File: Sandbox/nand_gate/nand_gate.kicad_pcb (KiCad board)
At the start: 2 copper layers, 63.5 x 33 mm, 11 parts, among them Q1 2N3904, Q2 2N3904, Q3 2N3904, SW1 SW_SPST, SW2 SW_SPST

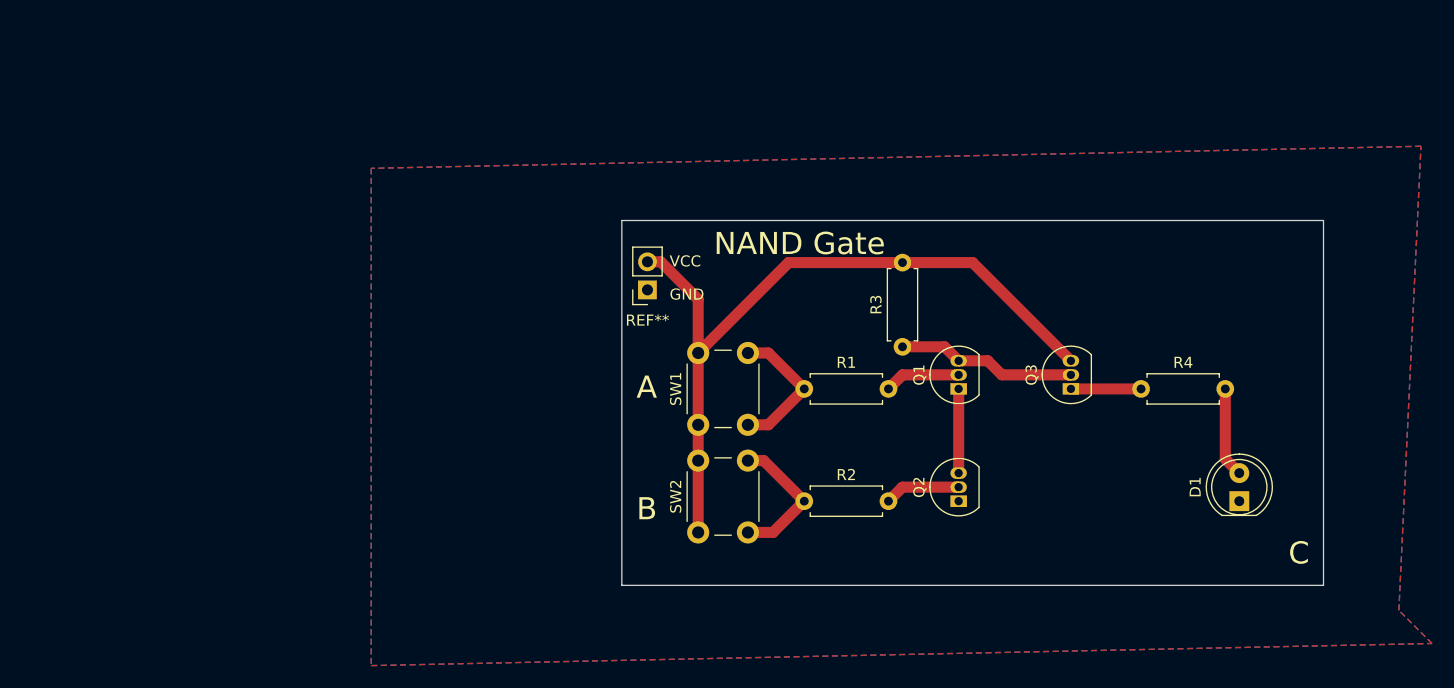
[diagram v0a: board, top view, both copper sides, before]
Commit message: Layout for nand gate
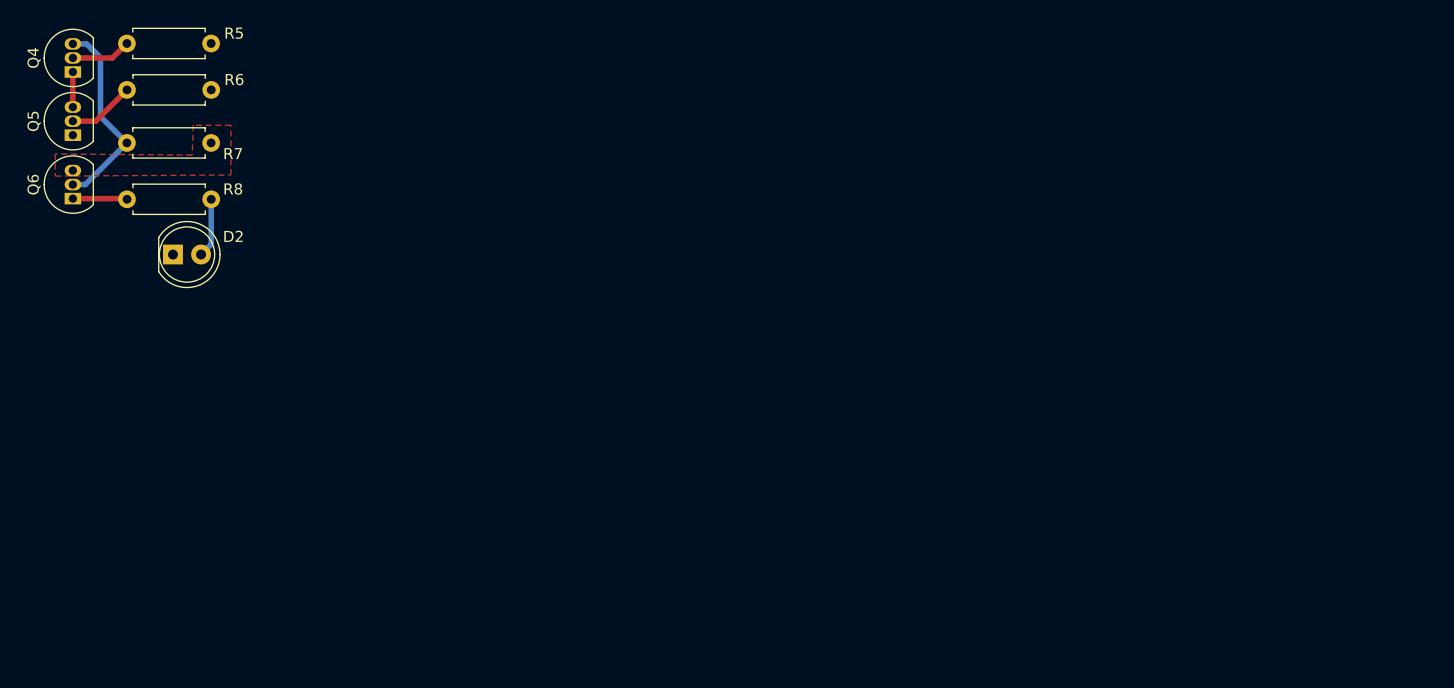
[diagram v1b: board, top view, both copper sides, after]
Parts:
- removed D1: LED, LED_THT:LED_D5.0mm
- removed Q1, Q2, Q3: 2N3904, Package_TO_SOT_THT:TO-92_Inline
- removed R1, R2, R3: 1k, Resistor_THT:R_Axial_DIN0207_L6.3mm_D2.5mm_P7.62mm_Horizontal
- removed R4: 150, Resistor_THT:R_Axial_DIN0207_L6.3mm_D2.5mm_P7.62mm_Horizontal
- removed REF**: PinSocket_1x02_P2.54mm_Vertical, Connector_PinSocket_2.54mm:PinSocket_1x02_P2.54mm_Vertical
- removed SW1, SW2: SW_SPST, Button_Switch_THT:SW_PUSH_6mm
- added D2: LED, LED_THT:LED_D5.0mm, F.Cu at (66.1, 48.8)
- added Q4: 2N3904, Package_TO_SOT_THT:TO-92_Inline, F.Cu at (57.0, 32.3)
- added Q5: 2N3904, Package_TO_SOT_THT:TO-92_Inline, F.Cu at (57.0, 38.0)
- added Q6: 2N3904, Package_TO_SOT_THT:TO-92_Inline, F.Cu at (57.0, 43.7)
- added R5: 1k, Resistor_THT:R_Axial_DIN0207_L6.3mm_D2.5mm_P7.62mm_Horizontal, F.Cu at (69.5, 29.7)
- added R6: 1k, Resistor_THT:R_Axial_DIN0207_L6.3mm_D2.5mm_P7.62mm_Horizontal, F.Cu at (69.5, 33.9)
- added R7: 1k, Resistor_THT:R_Axial_DIN0207_L6.3mm_D2.5mm_P7.62mm_Horizontal, F.Cu at (61.9, 38.7)
- added R8: 150, Resistor_THT:R_Axial_DIN0207_L6.3mm_D2.5mm_P7.62mm_Horizontal, F.Cu at (61.9, 43.8)
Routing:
- net VCC: track 67.9 -> 0.00 mm
- net Net-(Q4-C): track 0.00 -> 18.2 mm
- net Net-(Q1-C): track 16.3 -> 0.00 mm
- net /B: track 13.5 -> 0.00 mm
- net /A: track 12.9 -> 0.00 mm
- net /C: track 8.15 -> 0.00 mm
- net Net-(Q1-E): track 7.62 -> 0.00 mm
- net Net-(Q2-B): track 6.88 -> 0.00 mm
- net Net-(Q1-B): track 6.88 -> 0.00 mm
- net Net-(Q3-E): track 6.35 -> 0.00 mm
- net Net-(Q5-B): track 0.00 -> 6.07 mm
- net Net-(Q4-B): track 0.00 -> 5.43 mm
- net /D-Flip Flop/D-Latch/SR-Latch/nand_gate/C: track 0.00 -> 5.38 mm
- net Net-(Q6-E): track 0.00 -> 4.92 mm
- net Net-(Q4-E): track 0.00 -> 3.18 mm
- added copper zone on F.Cu, net VCC
- removed copper zone on B.Cu, net GND
- removed copper zone on F.Cu, net GND
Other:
- board outline removed
- board text removed: "A"
- board text removed: "B"
- board text removed: "C"
- board text removed: "GND"
- board text removed: "NAND GATE -------- A, B = C 0, 0, 1 0, 1, 1 1, 0, 1 1, 1, 0"
- board text removed: "NAND Gate"
- board text removed: "VCC"

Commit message: D-Latch Done
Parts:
- added D1: LED, LED_THT:LED_D5.0mm, F.Cu at (58.7, 49.0)
- added D3: LED, LED_THT:LED_D5.0mm, F.Cu at (44.3, 49.4)
- added D4: LED, LED_THT:LED_D5.0mm, F.Cu at (38.6, 50.2)
- added D5: LED, LED_THT:LED_D5.0mm, F.Cu at (86.6, 49.1)
- added Q1: 2N3904, Package_TO_SOT_THT:TO-92_Inline, F.Cu at (67.8, 65.6)
- added Q10: 2N3904, Package_TO_SOT_THT:TO-92_Inline, F.Cu at (47.7, 66.7)
- added Q11: 2N3904, Package_TO_SOT_THT:TO-92_Inline, F.Cu at (47.7, 61.0)
- added Q12: 2N3904, Package_TO_SOT_THT:TO-92_Inline, F.Cu at (47.7, 55.3)
- added Q13: 2N3904, Package_TO_SOT_THT:TO-92_Inline, F.Cu at (77.5, 32.6)
- added Q14: 2N3904, Package_TO_SOT_THT:TO-92_Inline, F.Cu at (77.5, 38.3)
- added Q15: 2N3904, Package_TO_SOT_THT:TO-92_Inline, F.Cu at (77.5, 44.0)
- added Q2: 2N3904, Package_TO_SOT_THT:TO-92_Inline, F.Cu at (67.8, 59.8)
- added Q3: 2N3904, Package_TO_SOT_THT:TO-92_Inline, F.Cu at (67.8, 54.1)
- added Q7: 2N3904, Package_TO_SOT_THT:TO-92_Inline, F.Cu at (35.2, 32.9)
- added Q8: 2N3904, Package_TO_SOT_THT:TO-92_Inline, F.Cu at (35.2, 38.6)
- added Q9: 2N3904, Package_TO_SOT_THT:TO-92_Inline, F.Cu at (35.2, 44.3)
- added R1: 1k, Resistor_THT:R_Axial_DIN0207_L6.3mm_D2.5mm_P7.62mm_Horizontal, F.Cu at (55.3, 68.1)
- added R10: 1k, Resistor_THT:R_Axial_DIN0207_L6.3mm_D2.5mm_P7.62mm_Horizontal, F.Cu at (47.7, 34.5)
- added R11: 1k, Resistor_THT:R_Axial_DIN0207_L6.3mm_D2.5mm_P7.62mm_Horizontal, F.Cu at (40.1, 39.3)
- added R12: 150, Resistor_THT:R_Axial_DIN0207_L6.3mm_D2.5mm_P7.62mm_Horizontal, F.Cu at (40.1, 44.4)
- added R13: 1k, Resistor_THT:R_Axial_DIN0207_L6.3mm_D2.5mm_P7.62mm_Horizontal, F.Cu at (35.2, 69.3)
- added R14: 1k, Resistor_THT:R_Axial_DIN0207_L6.3mm_D2.5mm_P7.62mm_Horizontal, F.Cu at (35.2, 65.1)
- added R15: 1k, Resistor_THT:R_Axial_DIN0207_L6.3mm_D2.5mm_P7.62mm_Horizontal, F.Cu at (42.8, 60.3)
- added R16: 150, Resistor_THT:R_Axial_DIN0207_L6.3mm_D2.5mm_P7.62mm_Horizontal, F.Cu at (42.8, 55.2)
- added R17: 1k, Resistor_THT:R_Axial_DIN0207_L6.3mm_D2.5mm_P7.62mm_Horizontal, F.Cu at (90.0, 30.0)
- added R18: 1k, Resistor_THT:R_Axial_DIN0207_L6.3mm_D2.5mm_P7.62mm_Horizontal, F.Cu at (90.0, 34.2)
- added R19: 1k, Resistor_THT:R_Axial_DIN0207_L6.3mm_D2.5mm_P7.62mm_Horizontal, F.Cu at (82.4, 39.0)
- added R2: 1k, Resistor_THT:R_Axial_DIN0207_L6.3mm_D2.5mm_P7.62mm_Horizontal, F.Cu at (55.3, 63.9)
- added R20: 150, Resistor_THT:R_Axial_DIN0207_L6.3mm_D2.5mm_P7.62mm_Horizontal, F.Cu at (82.4, 44.1)
- added R3: 1k, Resistor_THT:R_Axial_DIN0207_L6.3mm_D2.5mm_P7.62mm_Horizontal, F.Cu at (62.9, 59.1)
- added R4: 150, Resistor_THT:R_Axial_DIN0207_L6.3mm_D2.5mm_P7.62mm_Horizontal, F.Cu at (62.9, 54.0)
- added R9: 1k, Resistor_THT:R_Axial_DIN0207_L6.3mm_D2.5mm_P7.62mm_Horizontal, F.Cu at (47.7, 30.3)
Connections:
- net /D-Flip Flop/D-Latch/SR-Latch/nand_gate/C renamed /D-Flip Flop/D-Latch/Q
- R5 pad 1: /D-Flip Flop/D-Latch/SR-Latch/nand_gate/A -> /D-Flip Flop/D-Latch/SR-Latch/Set
- R6 pad 1: /D-Flip Flop/D-Latch/SR-Latch/nand_gate/B -> /D-Flip Flop/D-Latch/!Q
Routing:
- net /D-Flip Flop/D-Latch/nand_gate3/B: track 0.00 -> 123.7 mm
- net VCC: track 0.00 -> 115.0 mm
- net /D-Flip Flop/D-Latch/Data: track 0.00 -> 59.6 mm
- net /D-Flip Flop/D-Latch/Enable: track 0.00 -> 42.4 mm
- net /D-Flip Flop/D-Latch/SR-Latch/Set: track 0.00 -> 36.0 mm
- net /D-Flip Flop/D-Latch/SR-Latch/Reset: track 0.00 -> 32.3 mm
- net /D-Flip Flop/D-Latch/!Q: track 0.00 -> 31.4 mm
- net /D-Flip Flop/D-Latch/Q: track 5.38 -> 30.2 mm
- net Net-(Q13-C): track 0.00 -> 18.2 mm
- net Net-(Q7-C): track 0.00 -> 18.2 mm
- net Net-(Q10-C): track 0.00 -> 18.2 mm
- net Net-(Q1-C): track 0.00 -> 18.2 mm
- net Net-(Q14-B): track 0.00 -> 6.07 mm
- net Net-(Q11-B): track 0.00 -> 6.07 mm
- net Net-(Q8-B): track 0.00 -> 6.07 mm
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- removed copper zone on F.Cu, net VCC

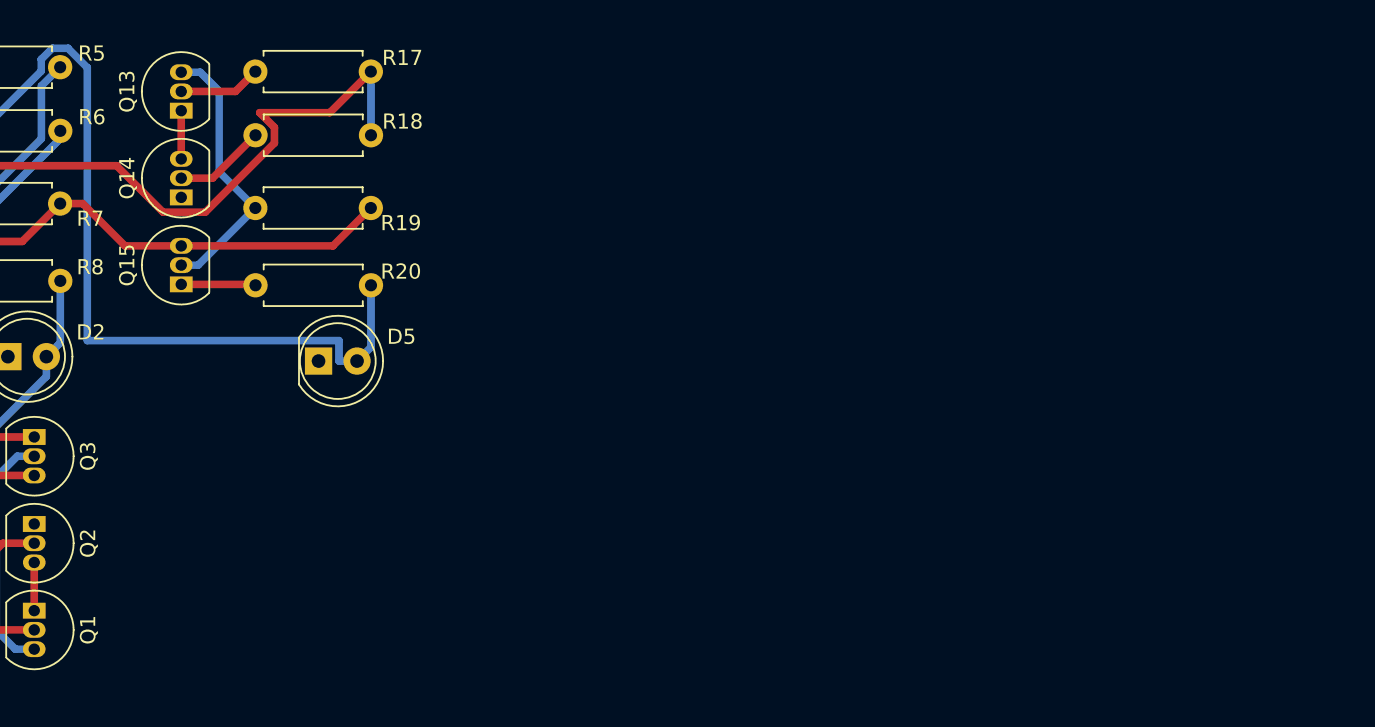
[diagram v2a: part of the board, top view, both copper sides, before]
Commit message: Added D Flip Flop
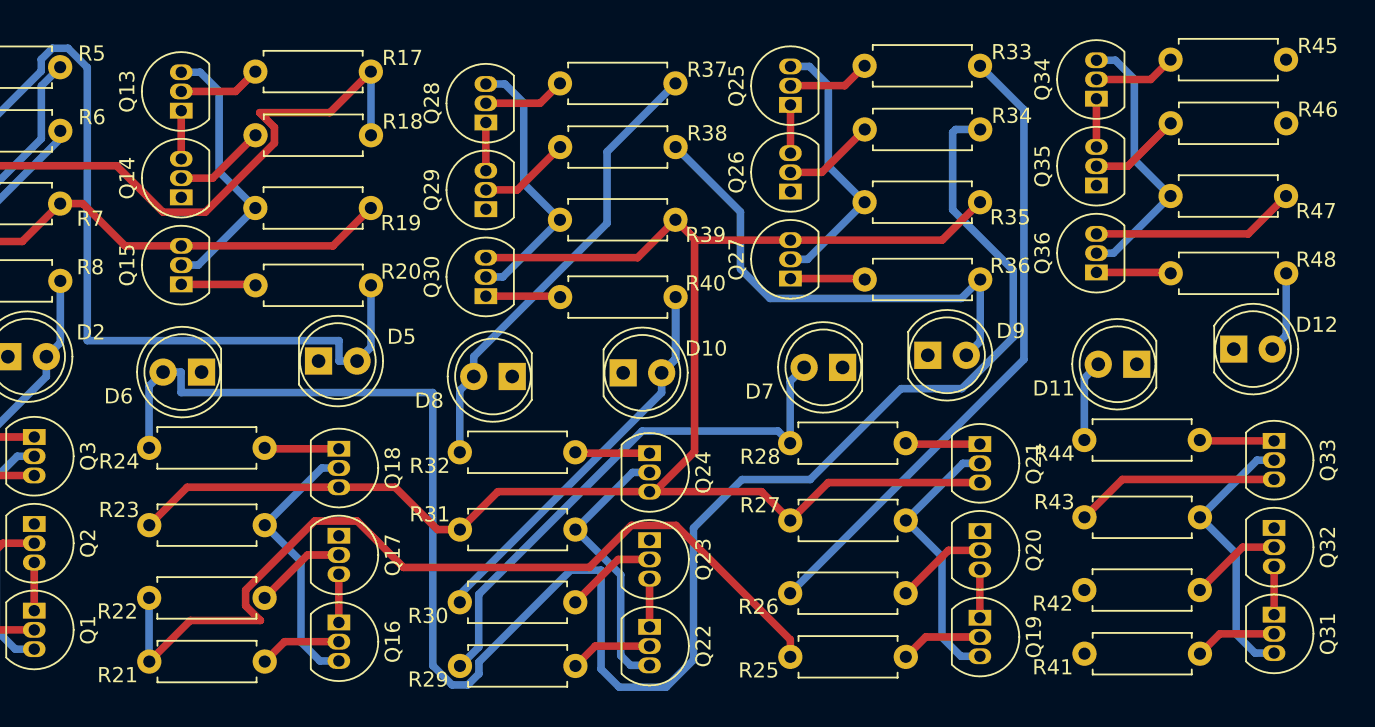
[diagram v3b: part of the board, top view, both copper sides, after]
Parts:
- added D10: LED, LED_THT:LED_D5.0mm, F.Cu at (106.7, 49.9)
- added D11: LED, LED_THT:LED_D5.0mm, F.Cu at (140.6, 49.3)
- added D12: LED, LED_THT:LED_D5.0mm, F.Cu at (146.9, 48.3)
- added D6: LED, LED_THT:LED_D5.0mm, F.Cu at (78.8, 49.8)
- added D7: LED, LED_THT:LED_D5.0mm, F.Cu at (121.1, 49.5)
- added D8: LED, LED_THT:LED_D5.0mm, F.Cu at (99.3, 50.1)
- added D9: LED, LED_THT:LED_D5.0mm, F.Cu at (126.8, 48.7)
- added Q16: 2N3904, Package_TO_SOT_THT:TO-92_Inline, F.Cu at (87.9, 66.3)
- added Q17: 2N3904, Package_TO_SOT_THT:TO-92_Inline, F.Cu at (87.9, 60.6)
- added Q18: 2N3904, Package_TO_SOT_THT:TO-92_Inline, F.Cu at (87.9, 54.9)
- added Q19: 2N3904, Package_TO_SOT_THT:TO-92_Inline, F.Cu at (130.2, 66.0)
- added Q20: 2N3904, Package_TO_SOT_THT:TO-92_Inline, F.Cu at (130.2, 60.3)
- added Q21: 2N3904, Package_TO_SOT_THT:TO-92_Inline, F.Cu at (130.2, 54.6)
- added Q22: 2N3904, Package_TO_SOT_THT:TO-92_Inline, F.Cu at (108.4, 66.6)
- added Q23: 2N3904, Package_TO_SOT_THT:TO-92_Inline, F.Cu at (108.4, 60.9)
- added Q24: 2N3904, Package_TO_SOT_THT:TO-92_Inline, F.Cu at (108.4, 55.2)
- added Q25: 2N3904, Package_TO_SOT_THT:TO-92_Inline, F.Cu at (117.7, 32.2)
- added Q26: 2N3904, Package_TO_SOT_THT:TO-92_Inline, F.Cu at (117.7, 37.9)
- added Q27: 2N3904, Package_TO_SOT_THT:TO-92_Inline, F.Cu at (117.7, 43.6)
- added Q28: 2N3904, Package_TO_SOT_THT:TO-92_Inline, F.Cu at (97.6, 33.3)
- added Q29: 2N3904, Package_TO_SOT_THT:TO-92_Inline, F.Cu at (97.6, 39.1)
- added Q30: 2N3904, Package_TO_SOT_THT:TO-92_Inline, F.Cu at (97.6, 44.8)
- added Q31: 2N3904, Package_TO_SOT_THT:TO-92_Inline, F.Cu at (149.6, 65.8)
- added Q32: 2N3904, Package_TO_SOT_THT:TO-92_Inline, F.Cu at (149.6, 60.1)
- added Q33: 2N3904, Package_TO_SOT_THT:TO-92_Inline, F.Cu at (149.6, 54.4)
- added Q34: 2N3904, Package_TO_SOT_THT:TO-92_Inline, F.Cu at (137.9, 31.8)
- added Q35: 2N3904, Package_TO_SOT_THT:TO-92_Inline, F.Cu at (137.9, 37.5)
- added Q36: 2N3904, Package_TO_SOT_THT:TO-92_Inline, F.Cu at (137.9, 43.2)
- added R21: 1k, Resistor_THT:R_Axial_DIN0207_L6.3mm_D2.5mm_P7.62mm_Horizontal, F.Cu at (75.4, 68.9)
- added R22: 1k, Resistor_THT:R_Axial_DIN0207_L6.3mm_D2.5mm_P7.62mm_Horizontal, F.Cu at (75.4, 64.7)
- added R23: 1k, Resistor_THT:R_Axial_DIN0207_L6.3mm_D2.5mm_P7.62mm_Horizontal, F.Cu at (83.0, 59.9)
- added R24: 150, Resistor_THT:R_Axial_DIN0207_L6.3mm_D2.5mm_P7.62mm_Horizontal, F.Cu at (83.0, 54.8)
- added R25: 1k, Resistor_THT:R_Axial_DIN0207_L6.3mm_D2.5mm_P7.62mm_Horizontal, F.Cu at (117.7, 68.6)
- added R26: 1k, Resistor_THT:R_Axial_DIN0207_L6.3mm_D2.5mm_P7.62mm_Horizontal, F.Cu at (117.7, 64.4)
- added R27: 1k, Resistor_THT:R_Axial_DIN0207_L6.3mm_D2.5mm_P7.62mm_Horizontal, F.Cu at (125.3, 59.6)
- added R28: 150, Resistor_THT:R_Axial_DIN0207_L6.3mm_D2.5mm_P7.62mm_Horizontal, F.Cu at (125.3, 54.5)
- added R29: 1k, Resistor_THT:R_Axial_DIN0207_L6.3mm_D2.5mm_P7.62mm_Horizontal, F.Cu at (95.9, 69.2)
- added R30: 1k, Resistor_THT:R_Axial_DIN0207_L6.3mm_D2.5mm_P7.62mm_Horizontal, F.Cu at (95.9, 65.0)
- added R31: 1k, Resistor_THT:R_Axial_DIN0207_L6.3mm_D2.5mm_P7.62mm_Horizontal, F.Cu at (103.5, 60.2)
- added R32: 150, Resistor_THT:R_Axial_DIN0207_L6.3mm_D2.5mm_P7.62mm_Horizontal, F.Cu at (103.5, 55.1)
- added R33: 1k, Resistor_THT:R_Axial_DIN0207_L6.3mm_D2.5mm_P7.62mm_Horizontal, F.Cu at (130.2, 29.6)
- added R34: 1k, Resistor_THT:R_Axial_DIN0207_L6.3mm_D2.5mm_P7.62mm_Horizontal, F.Cu at (130.2, 33.8)
- added R35: 1k, Resistor_THT:R_Axial_DIN0207_L6.3mm_D2.5mm_P7.62mm_Horizontal, F.Cu at (122.6, 38.6)
- added R36: 150, Resistor_THT:R_Axial_DIN0207_L6.3mm_D2.5mm_P7.62mm_Horizontal, F.Cu at (122.6, 43.7)
- added R37: 1k, Resistor_THT:R_Axial_DIN0207_L6.3mm_D2.5mm_P7.62mm_Horizontal, F.Cu at (110.1, 30.8)
- added R38: 1k, Resistor_THT:R_Axial_DIN0207_L6.3mm_D2.5mm_P7.62mm_Horizontal, F.Cu at (110.1, 35.0)
- added R39: 1k, Resistor_THT:R_Axial_DIN0207_L6.3mm_D2.5mm_P7.62mm_Horizontal, F.Cu at (102.5, 39.8)
- added R40: 150, Resistor_THT:R_Axial_DIN0207_L6.3mm_D2.5mm_P7.62mm_Horizontal, F.Cu at (102.5, 44.9)
- added R41: 1k, Resistor_THT:R_Axial_DIN0207_L6.3mm_D2.5mm_P7.62mm_Horizontal, F.Cu at (137.1, 68.4)
- added R42: 1k, Resistor_THT:R_Axial_DIN0207_L6.3mm_D2.5mm_P7.62mm_Horizontal, F.Cu at (137.1, 64.2)
- added R43: 1k, Resistor_THT:R_Axial_DIN0207_L6.3mm_D2.5mm_P7.62mm_Horizontal, F.Cu at (144.7, 59.4)
- added R44: 150, Resistor_THT:R_Axial_DIN0207_L6.3mm_D2.5mm_P7.62mm_Horizontal, F.Cu at (144.7, 54.3)
- added R45: 1k, Resistor_THT:R_Axial_DIN0207_L6.3mm_D2.5mm_P7.62mm_Horizontal, F.Cu at (150.4, 29.2)
- added R46: 1k, Resistor_THT:R_Axial_DIN0207_L6.3mm_D2.5mm_P7.62mm_Horizontal, F.Cu at (150.4, 33.4)
- added R47: 1k, Resistor_THT:R_Axial_DIN0207_L6.3mm_D2.5mm_P7.62mm_Horizontal, F.Cu at (142.8, 38.2)
- added R48: 150, Resistor_THT:R_Axial_DIN0207_L6.3mm_D2.5mm_P7.62mm_Horizontal, F.Cu at (142.8, 43.3)
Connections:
- net /D-Flip Flop/D-Latch/Data renamed /D-Flip Flop/Data
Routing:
- net VCC: track 115.0 -> 257.1 mm
- net /D-Flip Flop/D-Latch1/nand_gate3/B: track 0.00 -> 123.7 mm
- net /D-Flip Flop/D-Latch/Q: track 30.2 -> 89.8 mm
- net /D-Flip Flop/D-Latch1/Enable: track 0.00 -> 47.8 mm
- net /D-Flip Flop/D-Latch1/SR-Latch/Set: track 0.00 -> 36.0 mm
- net /D-Flip Flop/D-Latch1/SR-Latch/Reset: track 0.00 -> 32.3 mm
- net /D-Flip Flop/!Q: track 0.00 -> 31.4 mm
- net /D-Flip Flop/Q: track 0.00 -> 30.2 mm
- net Net-(Q34-C): track 0.00 -> 18.2 mm
- net Net-(Q31-C): track 0.00 -> 18.2 mm
- net Net-(Q16-C): track 0.00 -> 18.2 mm
- net Net-(Q28-C): track 0.00 -> 18.2 mm
- net Net-(Q22-C): track 0.00 -> 18.2 mm
- net Net-(Q25-C): track 0.00 -> 18.2 mm
- net Net-(Q19-C): track 0.00 -> 18.2 mm
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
